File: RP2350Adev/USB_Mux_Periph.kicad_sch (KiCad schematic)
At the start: 12 parts, among them J7 USB_A_Male, J8 USB_A_Female, J9 USB4105-GF-A, M1 TS3USB3031RMGR, SW1 SW_DIP_x06, U8 TS3USB30EDGSR

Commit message: Combine subcircuits
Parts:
- renumbered J7 to J701, J8 to J702, J9 to J703, M1 to M701, R18 to R701, R19 to R702, R20 to R703, R21 to R704, R22 to R705, R23 to R706, SW1 to SW701, U8 to U701
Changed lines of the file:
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@@
 		(dnp no)
 		(fields_autoplaced yes)
-		(property "Reference" "#PWR085"
+		(property "Reference" "#PWR0707"
 			(at 95.25 87.63 0)
 			(effects
@@
 			(project "RP2350Adev"
 				(path "/1f57b86c-11e7-4ea8-8f36-592c0861a25b/035fadad-9eba-4726-a427-88058f0933c7"
-					(reference "#PWR085")
+					(reference "#PWR0707")
 					(unit 1)
 				)
@@
 		(dnp no)
 		(fields_autoplaced yes)
-		(property "Reference" "#PWR088"
+		(property "Reference" "#PWR0710"
 			(at 147.32 66.04 0)
 			(effects
@@
 			(project "main"
 				(path "/1f57b86c-11e7-4ea8-8f36-592c0861a25b/035fadad-9eba-4726-a427-88058f0933c7"
-					(reference "#PWR088")
+					(reference "#PWR0710")
 					(unit 1)
 				)
@@
 		(dnp no)
 		(fields_autoplaced yes)
-		(property "Reference" "J8"
+		(property "Reference" "J702"
 			(at 49.53 66.04 0)
 			(effects
@@
 			(project ""
 				(path "/1f57b86c-11e7-4ea8-8f36-592c0861a25b/035fadad-9eba-4726-a427-88058f0933c7"
-					(reference "J8")
+					(reference "J702")
 					(unit 1)
 				)
@@
 		(dnp no)
 		(fields_autoplaced yes)
-		(property "Reference" "R22"
+		(property "Reference" "R705"
 			(at 256.54 54.6099 0)
 			(effects
@@
 			(project "main"
 				(path "/1f57b86c-11e7-4ea8-8f36-592c0861a25b/035fadad-9eba-4726-a427-88058f0933c7"
-					(reference "R22")
+					(reference "R705")
 					(unit 1)
 				)
@@
 		(dnp no)
 		(fields_autoplaced yes)
-		(property "Reference" "#PWR092"
+		(property "Reference" "#PWR0714"
 			(at 254 66.04 0)
 			(effects
@@
 			(project "main"
 				(path "/1f57b86c-11e7-4ea8-8f36-592c0861a25b/035fadad-9eba-4726-a427-88058f0933c7"
-					(reference "#PWR092")
+					(reference "#PWR0714")
 					(unit 1)
 				)
@@
 		(dnp no)
 		(fields_autoplaced yes)
-		(property "Reference" "J7"
+		(property "Reference" "J701"
 			(at 49.53 33.02 0)
 			(effects
@@
 			(project ""
 				(path "/1f57b86c-11e7-4ea8-8f36-592c0861a25b/035fadad-9eba-4726-a427-88058f0933c7"
-					(reference "J7")
+					(reference "J701")
 					(unit 1)
 				)
@@
 		(dnp no)
 		(fields_autoplaced yes)
-		(property "Reference" "R18"
+		(property "Reference" "R701"
 			(at 46.99 107.9499 0)
 			(effects
@@
 			(project "main"
 				(path "/1f57b86c-11e7-4ea8-8f36-592c0861a25b/035fadad-9eba-4726-a427-88058f0933c7"
-					(reference "R18")
+					(reference "R701")
 					(unit 1)
 				)
@@
 		(dnp no)
 		(fields_autoplaced yes)
-		(property "Reference" "#PWR087"
+		(property "Reference" "#PWR0709"
 			(at 142.24 85.09 0)
 			(effects
@@
 			(project "main"
 				(path "/1f57b86c-11e7-4ea8-8f36-592c0861a25b/035fadad-9eba-4726-a427-88058f0933c7"
-					(reference "#PWR087")
+					(reference "#PWR0709")
 					(unit 1)
 				)
@@
 		(on_board yes)
 		(dnp no)
-		(property "Reference" "#PWR091"
+		(property "Reference" "#PWR0713"
 			(at 248.92 68.58 0)
 			(effects
@@
 			(project "main"
 				(path "/1f57b86c-11e7-4ea8-8f36-592c0861a25b/035fadad-9eba-4726-a427-88058f0933c7"
-					(reference "#PWR091")
+					(reference "#PWR0713")
 					(unit 1)
 				)
@@
 		(dnp no)
 		(fields_autoplaced yes)
-		(property "Reference" "#PWR079"
+		(property "Reference" "#PWR0701"
 			(at 44.45 130.81 0)
 			(effects
@@
 			(project "main"
 				(path "/1f57b86c-11e7-4ea8-8f36-592c0861a25b/035fadad-9eba-4726-a427-88058f0933c7"
-					(reference "#PWR079")
+					(reference "#PWR0701")
 					(unit 1)
 				)
@@
 		(on_board yes)
 		(dnp no)
-		(property "Reference" "M1"
+		(property "Reference" "M701"
 			(at 170.18 52.07 0)
 			(effects
@@
 			(project "main"
 				(path "/1f57b86c-11e7-4ea8-8f36-592c0861a25b/035fadad-9eba-4726-a427-88058f0933c7"
-					(reference "M1")
+					(reference "M701")
 					(unit 1)
 				)
@@
 		(dnp no)
 		(fields_autoplaced yes)
-		(property "Reference" "R19"
+		(property "Reference" "R702"
 			(at 66.04 110.4899 0)
 			(effects
@@
 			(project "main"
 				(path "/1f57b86c-11e7-4ea8-8f36-592c0861a25b/035fadad-9eba-4726-a427-88058f0933c7"
-					(reference "R19")
+					(reference "R702")
 					(unit 1)
 				)
@@
 		(on_board yes)
 		(dnp no)
-		(property "Reference" "U8"
+		(property "Reference" "U701"
 			(at 93.1067 57.15 0)
 			(effects
@@
 			(project "RP2350Adev"
 				(path "/1f57b86c-11e7-4ea8-8f36-592c0861a25b/035fadad-9eba-4726-a427-88058f0933c7"
-					(reference "U8")
+					(reference "U701")
 					(unit 1)
 				)
@@
 		(dnp no)
 		(fields_autoplaced yes)
-		(property "Reference" "R23"
+		(property "Reference" "R706"
 			(at 265.43 54.6099 0)
 			(effects
@@
 			(project "main"
 				(path "/1f57b86c-11e7-4ea8-8f36-592c0861a25b/035fadad-9eba-4726-a427-88058f0933c7"
-					(reference "R23")
+					(reference "R706")
 					(unit 1)
 				)
@@
 		(dnp no)
 		(fields_autoplaced yes)
-		(property "Reference" "#PWR086"
+		(property "Reference" "#PWR0708"
 			(at 129.54 109.22 0)
 			(effects
@@
 			(project "main"
 				(path "/1f57b86c-11e7-4ea8-8f36-592c0861a25b/035fadad-9eba-4726-a427-88058f0933c7"
-					(reference "#PWR086")
+					(reference "#PWR0708")
 					(unit 1)
 				)
@@
 		(dnp no)
 		(fields_autoplaced yes)
-		(property "Reference" "#PWR084"
+		(property "Reference" "#PWR0706"
 			(at 95.25 60.96 0)
 			(effects
@@
 			(project "main"
 				(path "/1f57b86c-11e7-4ea8-8f36-592c0861a25b/035fadad-9eba-4726-a427-88058f0933c7"
-					(reference "#PWR084")
+					(reference "#PWR0706")
 					(unit 1)
 				)
@@
 		(dnp no)
 		(fields_autoplaced yes)
-		(property "Reference" "#PWR090"
+		(property "Reference" "#PWR0712"
 			(at 248.92 35.56 0)
 			(effects
@@
 			(project "main"
 				(path "/1f57b86c-11e7-4ea8-8f36-592c0861a25b/035fadad-9eba-4726-a427-88058f0933c7"
-					(reference "#PWR090")
+					(reference "#PWR0712")
 					(unit 1)
 				)
@@
 		(dnp no)
 		(fields_autoplaced yes)
-		(property "Reference" "#PWR093"
+		(property "Reference" "#PWR0715"
 			(at 262.89 66.04 0)
 			(effects
@@
 			(project "main"
 				(path "/1f57b86c-11e7-4ea8-8f36-592c0861a25b/035fadad-9eba-4726-a427-88058f0933c7"
-					(reference "#PWR093")
+					(reference "#PWR0715")
 					(unit 1)
 				)
@@
 		(dnp no)
 		(fields_autoplaced yes)
-		(property "Reference" "R20"
+		(property "Reference" "R703"
 			(at 85.09 113.0299 0)
 			(effects
@@
 			(project "main"
 				(path "/1f57b86c-11e7-4ea8-8f36-592c0861a25b/035fadad-9eba-4726-a427-88058f0933c7"
-					(reference "R20")
+					(reference "R703")
 					(unit 1)
 				)
@@
 		(dnp no)
 		(fields_autoplaced yes)
-		(property "Reference" "R21"
+		(property "Reference" "R704"
 			(at 102.87 115.5699 0)
 			(effects
@@
 			(project "main"
 				(path "/1f57b86c-11e7-4ea8-8f36-592c0861a25b/035fadad-9eba-4726-a427-88058f0933c7"
-					(reference "R21")
+					(reference "R704")
 					(unit 1)
 				)
@@
 		(dnp no)
 		(fields_autoplaced yes)
-		(property "Reference" "#PWR080"
+		(property "Reference" "#PWR0702"
 			(at 46.99 63.5 0)
 			(effects
@@
 			(project "RP2350Adev"
 				(path "/1f57b86c-11e7-4ea8-8f36-592c0861a25b/035fadad-9eba-4726-a427-88058f0933c7"
-					(reference "#PWR080")
+					(reference "#PWR0702")
 					(unit 1)
 				)
@@
 		(on_board yes)
 		(dnp no)
-		(property "Reference" "J9"
+		(property "Reference" "J703"
 			(at 223.52 25.4 0)
 			(effects
@@
 			(project "main"
 				(path "/1f57b86c-11e7-4ea8-8f36-592c0861a25b/035fadad-9eba-4726-a427-88058f0933c7"
-					(reference "J9")
+					(reference "J703")
 					(unit 1)
 				)
@@
 		(dnp no)
 		(fields_autoplaced yes)
-		(property "Reference" "#PWR083"
+		(property "Reference" "#PWR0705"
 			(at 59.69 73.66 0)
 			(effects
@@
 			(project "RP2350Adev"
 				(path "/1f57b86c-11e7-4ea8-8f36-592c0861a25b/035fadad-9eba-4726-a427-88058f0933c7"
-					(reference "#PWR083")
+					(reference "#PWR0705")
 					(unit 1)
 				)
@@
 		(dnp no)
 		(fields_autoplaced yes)
-		(property "Reference" "#PWR081"
+		(property "Reference" "#PWR0703"
 			(at 46.99 96.52 0)
 			(effects
@@
 			(project "RP2350Adev"
 				(path "/1f57b86c-11e7-4ea8-8f36-592c0861a25b/035fadad-9eba-4726-a427-88058f0933c7"
-					(reference "#PWR081")
+					(reference "#PWR0703")
 					(unit 1)
 				)
@@
 		(dnp no)
 		(fields_autoplaced yes)
-		(property "Reference" "#PWR082"
+		(property "Reference" "#PWR0704"
 			(at 59.69 40.64 0)
 			(effects
@@
 			(project "main"
 				(path "/1f57b86c-11e7-4ea8-8f36-592c0861a25b/035fadad-9eba-4726-a427-88058f0933c7"
-					(reference "#PWR082")
+					(reference "#PWR0704")
 					(unit 1)
 				)
@@
 		(dnp no)
 		(fields_autoplaced yes)
-		(property "Reference" "#PWR089"
+		(property "Reference" "#PWR0711"
 			(at 226.06 78.74 0)
 			(effects
@@
 			(project "main"
 				(path "/1f57b86c-11e7-4ea8-8f36-592c0861a25b/035fadad-9eba-4726-a427-88058f0933c7"
-					(reference "#PWR089")
+					(reference "#PWR0711")
 					(unit 1)
 				)
@@
 		(on_board yes)
 		(dnp no)
-		(property "Reference" "SW1"
+		(property "Reference" "SW701"
 			(at 115.57 97.79 0)
 			(effects
@@
 			(project "main"
 				(path "/1f57b86c-11e7-4ea8-8f36-592c0861a25b/035fadad-9eba-4726-a427-88058f0933c7"
-					(reference "SW1")
-					(unit 1)
-				)
+					(reference "SW701")
+					(unit 1)
+				)

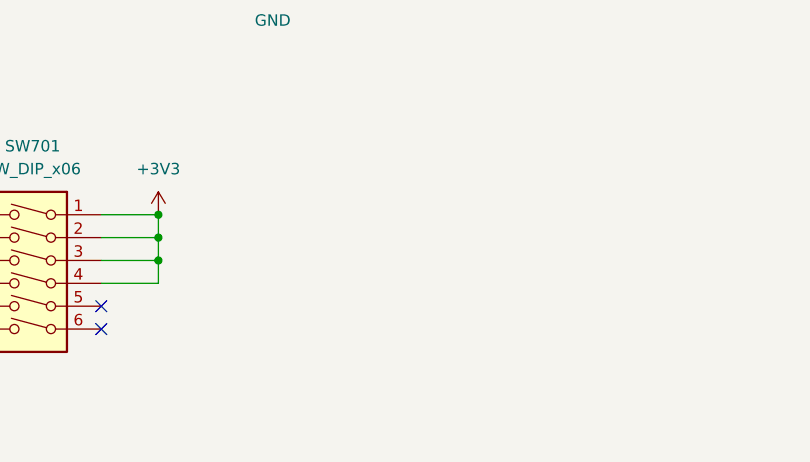
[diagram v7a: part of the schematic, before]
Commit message: fix footprint errors
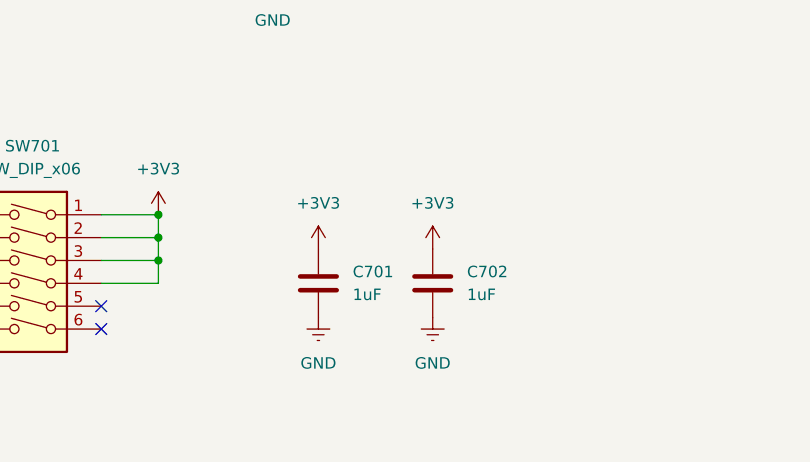
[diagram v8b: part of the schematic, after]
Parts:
- added C701, C702: 1uF, Capacitor_SMD:C_0402_1005Metric, symbol Device:C
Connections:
- net +3V3: now also C701.2, C702.2
- net GND: now also C701.1, C702.1
